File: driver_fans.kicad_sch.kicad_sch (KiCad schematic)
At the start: 9 parts, among them Q3 2N7002, U1 EL3H7

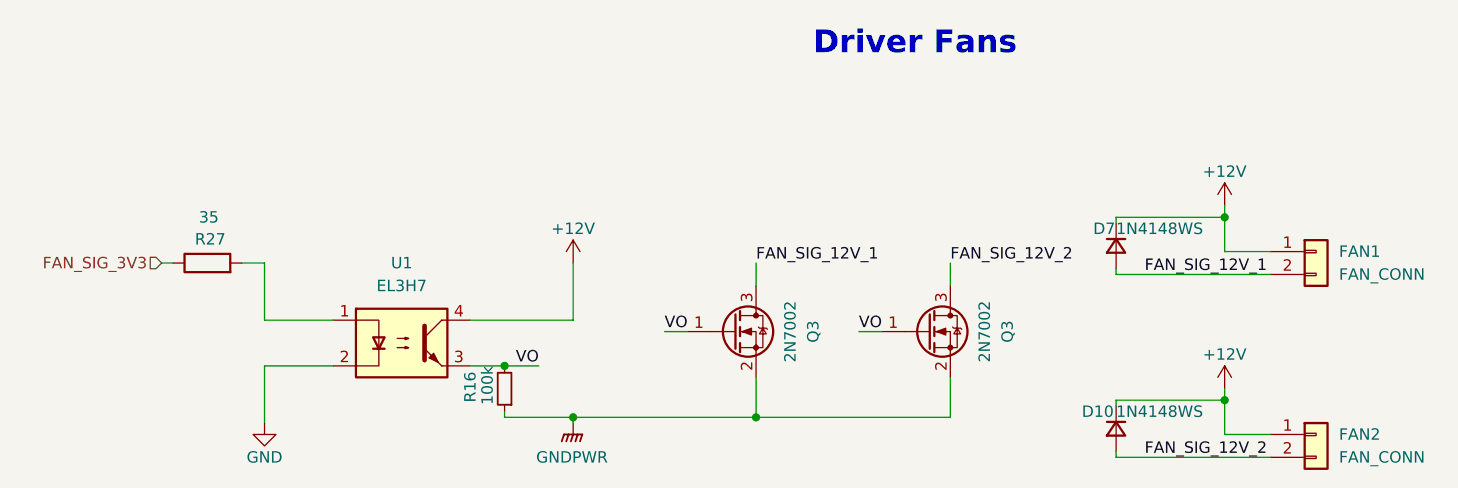
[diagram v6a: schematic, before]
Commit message: Added test points
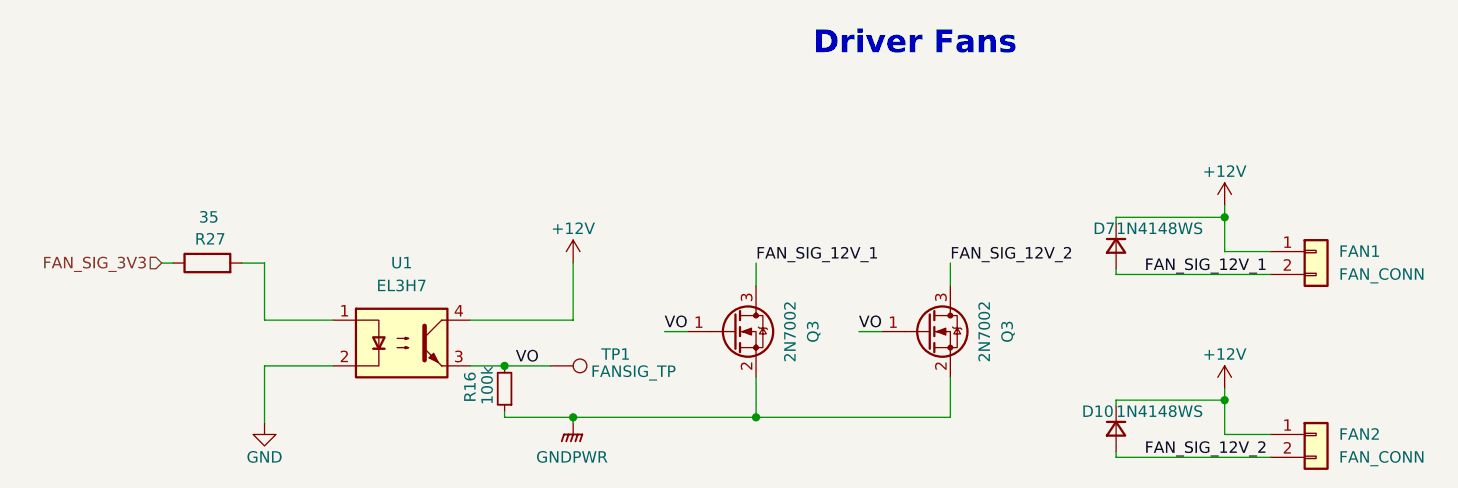
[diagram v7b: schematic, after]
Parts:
- added TP1: FANSIG_TP, symbol Connector:TestPoint
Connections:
- net VO: now also TP1.1
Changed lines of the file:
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@@
     (stroke (width 0) (type default))
   )
-  (wire (pts (xy 95.25 101.6) (xy 99.06 101.6))
+  (wire (pts (xy 95.25 101.6) (xy 100.33 101.6))
     (stroke (width 0) (type default))
   )
@@
         )
       )
+    )
+  )
+  (symbol (lib_id "Connector:TestPoint") (at 100.33 101.6 270) (unit 1)
+    (in_bom yes) (on_board yes) (dnp no)
+    (property "Reference" "TP1" (at 109.22 100.33 90)
+      (effects (font (size 1.27 1.27)) (justify right))
+    )
+    (property "Value" "FANSIG_TP" (at 114.3 102.235 90)
+      (effects (font (size 1.27 1.27)) (justify right))
+    )
+    (property "Footprint" "" (at 100.33 106.68 0)
+      (effects (font (size 1.27 1.27)) hide)
+    )
+    (property "Datasheet" "~" (at 100.33 106.68 0)
+      (effects (font (size 1.27 1.27)) hide)
+    )
+    (pin "1")
+    (instances
+      (project "Controls-LeaderDaughterPCB"
+        (path "/c7871779-04fe-4705-8150-20a4dd0ef44f"
+          (reference "TP1") (unit 1)
+        )
+        (path "/c7871779-04fe-4705-8150-20a4dd0ef44f/fd5723b9-3644-4daa-af29-4c44667f673c"
+          (reference "TP11") (unit 1)
+        )
+      )

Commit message: Adjusted & added footprints, several minor changes
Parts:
- TP1: footprint (none) -> TestPoint:TestPoint_Pad_1.5x1.5mm
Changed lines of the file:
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@@
       (effects (font (size 1.27 1.27)) (justify right))
     )
-    (property "Footprint" "" (at 100.33 106.68 0)
+    (property "Footprint" "TestPoint:TestPoint_Pad_1.5x1.5mm" (at 100.33 106.68 0)
       (effects (font (size 1.27 1.27)) hide)
     )
